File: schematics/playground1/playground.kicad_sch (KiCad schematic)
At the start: 98 parts, among them J1 Conn_01x05, J2 Conn_02x03_Odd_Even, J3 Conn_01x03, J4 Conn_02x04_Odd_Even, SW1 SW_SPST, SW2 SW_Push, SW3 SW_Push, U1 ADS1299, U2 MCP1700x-330xxTT, U3 PIC32MX250F128B_I_SS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

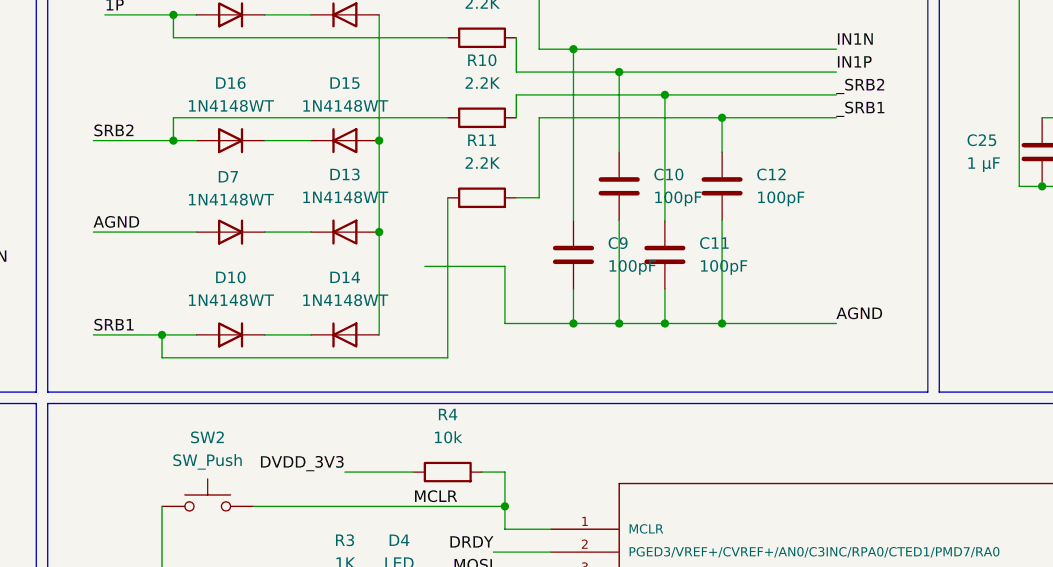
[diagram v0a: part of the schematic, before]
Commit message: add tracing for new resistor / diode arrays
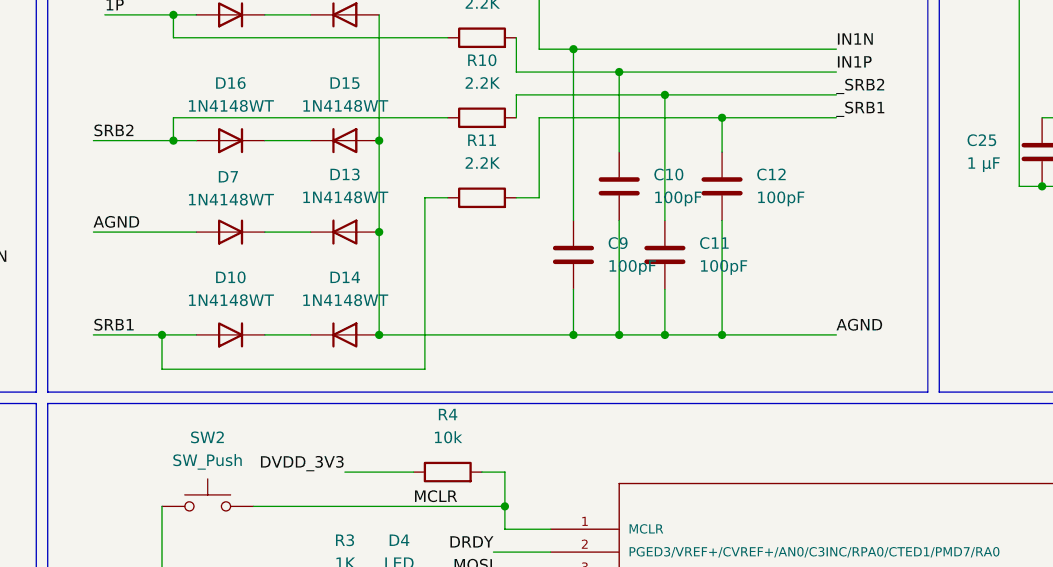
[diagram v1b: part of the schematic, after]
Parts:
- R10, R11, R8, R9: footprint (none) -> Resistor_SMD:R_0603_1608Metric
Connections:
- net AGND: now also D12.2 (A), D13.2 (A), D14.2 (A), D15.2 (A)
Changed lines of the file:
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@@
 	)
 	(junction
-		(at 153.67 162.56)
-		(diameter 0)
-		(color 0 0 0 0)
-	)
-	(junction
 		(at 251.46 45.72)
 		(diameter 0)
@@
 	)
 	(junction
-		(at 147.32 162.56)
-		(diameter 0)
-		(color 0 0 0 0)
-	)
-	(junction
 		(at 110.49 222.25)
 		(diameter 0)
@@
 	)
 	(junction
+		(at 137.16 163.83)
+		(diameter 0)
+		(color 0 0 0 0)
+	)
+	(junction
 		(at 91.44 86.36)
 		(diameter 0)
@@
 	)
 	(junction
-		(at 142.24 162.56)
-		(diameter 0)
-		(color 0 0 0 0)
-	)
-	(junction
 		(at 109.22 210.82)
 		(diameter 0)
@@
 	)
 	(junction
-		(at 137.16 162.56)
+		(at 281.94 115.57)
 		(diameter 0)
 		(color 0 0 0 0)
 	)
 	(junction
-		(at 281.94 115.57)
+		(at 91.44 163.83)
 		(diameter 0)
 		(color 0 0 0 0)
 	)
 	(junction
-		(at 91.44 163.83)
+		(at 142.24 163.83)
 		(diameter 0)
 		(color 0 0 0 0)
@@
 	)
 	(junction
+		(at 147.32 163.83)
+		(diameter 0)
+		(color 0 0 0 0)
+	)
+	(junction
 		(at 278.13 87.63)
 		(diameter 0)
@@
 	)
 	(junction
+		(at 115.57 163.83)
+		(diameter 0)
+		(color 0 0 0 0)
+	)
+	(junction
 		(at 91.44 43.18)
 		(diameter 0)
@@
 	)
 	(junction
+		(at 153.67 163.83)
+		(diameter 0)
+		(color 0 0 0 0)
+	)
+	(junction
 		(at 120.65 43.18)
 		(diameter 0)
@@
 	(wire
 		(pts
-			(xy 142.24 162.56) (xy 147.32 162.56)
+			(xy 142.24 163.83) (xy 147.32 163.83)
 		)
 		(stroke
@@
 	(wire
 		(pts
-			(xy 147.32 158.75) (xy 147.32 162.56)
-		)
-		(stroke
-			(width 0)
-			(type default)
-		)
-	)
-	(wire
-		(pts
 			(xy 208.28 147.32) (xy 219.71 147.32)
 		)
@@
 	(wire
 		(pts
-			(xy 120.65 156.21) (xy 129.54 156.21)
-		)
-		(stroke
-			(width 0)
-			(type default)
-		)
-	)
-	(wire
-		(pts
 			(xy 100.33 199.39) (xy 100.33 201.93)
 		)
@@
 	(wire
 		(pts
+			(xy 115.57 163.83) (xy 137.16 163.83)
+		)
+		(stroke
+			(width 0)
+			(type default)
+		)
+	)
+	(wire
+		(pts
 			(xy 116.84 43.18) (xy 120.65 43.18)
 		)
@@
 	(wire
 		(pts
-			(xy 91.44 163.83) (xy 91.44 166.37)
+			(xy 91.44 163.83) (xy 91.44 167.64)
 		)
 		(stroke
@@
 	(wire
 		(pts
-			(xy 129.54 162.56) (xy 137.16 162.56)
+			(xy 153.67 163.83) (xy 166.37 163.83)
 		)
 		(stroke
@@
 	(wire
 		(pts
-			(xy 153.67 162.56) (xy 166.37 162.56)
+			(xy 109.22 68.58) (xy 109.22 63.5)
 		)
 		(stroke
@@
 	(wire
 		(pts
-			(xy 109.22 68.58) (xy 109.22 63.5)
+			(xy 153.67 151.13) (xy 153.67 163.83)
 		)
 		(stroke
@@
 	(wire
 		(pts
-			(xy 153.67 162.56) (xy 153.67 151.13)
+			(xy 147.32 137.16) (xy 166.37 137.16)
 		)
 		(stroke
@@
 	(wire
 		(pts
-			(xy 147.32 137.16) (xy 166.37 137.16)
+			(xy 149.86 59.69) (xy 149.86 62.23)
 		)
 		(stroke
@@
 	(wire
 		(pts
-			(xy 149.86 59.69) (xy 149.86 62.23)
+			(xy 323.85 83.82) (xy 323.85 87.63)
 		)
 		(stroke
@@
 	(wire
 		(pts
-			(xy 323.85 83.82) (xy 323.85 87.63)
+			(xy 127 100.33) (xy 120.65 100.33)
 		)
 		(stroke
@@
 	(wire
 		(pts
-			(xy 127 100.33) (xy 120.65 100.33)
+			(xy 39.37 92.71) (xy 45.72 92.71)
 		)
 		(stroke
@@
 	(wire
 		(pts
-			(xy 39.37 92.71) (xy 45.72 92.71)
+			(xy 137.16 163.83) (xy 142.24 163.83)
 		)
 		(stroke
@@
 	(wire
 		(pts
-			(xy 137.16 162.56) (xy 142.24 162.56)
+			(xy 120.65 43.18) (xy 120.65 53.34)
 		)
 		(stroke
@@
 	(wire
 		(pts
-			(xy 120.65 43.18) (xy 120.65 53.34)
+			(xy 137.16 158.75) (xy 137.16 163.83)
 		)
 		(stroke
@@
 	(wire
 		(pts
-			(xy 147.32 162.56) (xy 153.67 162.56)
+			(xy 147.32 163.83) (xy 153.67 163.83)
 		)
 		(stroke
@@
 	(wire
 		(pts
-			(xy 142.24 151.13) (xy 142.24 162.56)
+			(xy 142.24 151.13) (xy 142.24 163.83)
 		)
 		(stroke
@@
 	(wire
 		(pts
+			(xy 147.32 158.75) (xy 147.32 163.83)
+		)
+		(stroke
+			(width 0)
+			(type default)
+		)
+	)
+	(wire
+		(pts
 			(xy 269.24 203.2) (xy 281.94 203.2)
 		)
@@
 	(wire
 		(pts
+			(xy 120.65 148.59) (xy 123.19 148.59)
+		)
+		(stroke
+			(width 0)
+			(type default)
+		)
+	)
+	(wire
+		(pts
 			(xy 91.44 80.01) (xy 101.6 80.01)
 		)
@@
 	(wire
 		(pts
-			(xy 123.19 166.37) (xy 91.44 166.37)
+			(xy 120.65 167.64) (xy 91.44 167.64)
 		)
 		(stroke
@@
 	(wire
 		(pts
-			(xy 137.16 158.75) (xy 137.16 162.56)
-		)
-		(stroke
-			(width 0)
-			(type default)
-		)
-	)
-	(wire
-		(pts
 			(xy 194.31 116.84) (xy 231.14 116.84)
 		)
@@
 	(wire
 		(pts
-			(xy 123.19 148.59) (xy 123.19 166.37)
+			(xy 120.65 148.59) (xy 120.65 167.64)
 		)
 		(stroke
@@
 	(wire
 		(pts
-			(xy 129.54 156.21) (xy 129.54 162.56)
-		)
-		(stroke
-			(width 0)
-			(type default)
-		)
-	)
-	(wire
-		(pts
 			(xy 248.92 144.78) (xy 246.38 144.78)
 		)
@@
 	)
 	(label "AGND"
-		(at 166.37 162.56 0)
+		(at 166.37 163.83 0)
 		(effects
 			(font
@@
 			)
 		)
-		(property "Footprint" ""
+		(property "Footprint" "Resistor_SMD:R_0603_1608Metric"
 			(at 127 150.368 90)
 			(effects
@@
 			)
 		)
-		(property "Footprint" ""
+		(property "Footprint" "Resistor_SMD:R_0603_1608Metric"
 			(at 127 123.698 90)
 			(effects
@@
 			)
 		)
-		(property "Footprint" ""
+		(property "Footprint" "Resistor_SMD:R_0603_1608Metric"
 			(at 127 141.478 90)
 			(effects
@@
 			)
 		)
-		(property "Footprint" ""
+		(property "Footprint" "Resistor_SMD:R_0603_1608Metric"
 			(at 127 132.588 90)
 			(effects

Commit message: traced pcb audio subsys edits
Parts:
- removed R6: 1k, Resistor_SMD:R_0603_1608Metric, symbol Device:R
- removed R7: 100k, Resistor_SMD:R_0603_1608Metric, symbol Device:R
- C40: value 1uF -> 0.1uF
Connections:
- net at U6.8 (VA): now also C40.1
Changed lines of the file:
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@@
 	)
 	(junction
-		(at 368.3 189.23)
-		(diameter 0)
-		(color 0 0 0 0)
-	)
-	(junction
 		(at 189.23 107.95)
 		(diameter 0)
@@
 	(wire
 		(pts
-			(xy 368.3 168.91) (xy 368.3 167.64)
-		)
-		(stroke
-			(width 0)
-			(type default)
-		)
-	)
-	(wire
-		(pts
 			(xy 100.33 199.39) (xy 100.33 201.93)
 		)
@@
 	(wire
 		(pts
-			(xy 347.98 189.23) (xy 356.87 189.23)
-		)
-		(stroke
-			(width 0)
-			(type default)
-		)
-	)
-	(wire
-		(pts
 			(xy 45.72 90.17) (xy 39.37 90.17)
 		)
@@
 	(wire
 		(pts
+			(xy 368.3 167.64) (xy 368.3 177.8)
+		)
+		(stroke
+			(width 0)
+			(type default)
+		)
+	)
+	(wire
+		(pts
 			(xy 130.81 130.81) (xy 130.81 134.62)
 		)
@@
 	(wire
 		(pts
-			(xy 368.3 176.53) (xy 368.3 177.8)
-		)
-		(stroke
-			(width 0)
-			(type default)
-		)
-	)
-	(wire
-		(pts
 			(xy 120.65 208.28) (xy 134.62 208.28)
 		)
@@
 	(wire
 		(pts
-			(xy 364.49 189.23) (xy 368.3 189.23)
-		)
-		(stroke
-			(width 0)
-			(type default)
-		)
-	)
-	(wire
-		(pts
 			(xy 100.33 210.82) (xy 109.22 210.82)
 		)
@@
 	)
 	(symbol
-		(lib_id "Device:R")
-		(at 368.3 172.72 0)
-		(unit 1)
-		(exclude_from_sim no)
-		(in_bom yes)
-		(on_board yes)
-		(dnp no)
-		(fields_autoplaced yes)
-		(property "Reference" "R6"
-			(at 370.84 171.4499 0)
-			(effects
-				(font
-					(size 1.27 1.27)
-				)
-				(justify left)
-			)
-		)
-		(property "Value" "1k"
-			(at 370.84 173.9899 0)
-			(effects
-				(font
-					(size 1.27 1.27)
-				)
-				(justify left)
-			)
-		)
-		(property "Footprint" "Resistor_SMD:R_0603_1608Metric"
-			(at 366.522 172.72 90)
-			(effects
-				(font
-					(size 1.27 1.27)
-				)
-				(hide yes)
-			)
-		)
-		(property "Datasheet" "~"
-			(at 368.3 172.72 0)
-			(effects
-				(font
-					(size 1.27 1.27)
-				)
-				(hide yes)
-			)
-		)
-		(property "Description" "Resistor"
-			(at 368.3 172.72 0)
-			(effects
-				(font
-					(size 1.27 1.27)
-				)
-				(hide yes)
-			)
-		)
-		(pin "2"
-		)
-		(pin "1"
-		)
-		(instances
-			(project "playground"
-				(path "/238de170-6a90-40ad-afaf-ab931b754487"
-					(reference "R6")
-					(unit 1)
-				)
-			)
-		)
-	)
-	(symbol
 		(lib_id "ble_symbols:C")
 		(at 200.66 135.89 0)
@@
 	)
 	(symbol
-		(lib_id "Device:R")
-		(at 360.68 189.23 270)
-		(mirror x)
-		(unit 1)
-		(exclude_from_sim no)
-		(in_bom yes)
-		(on_board yes)
-		(dnp no)
-		(property "Reference" "R7"
-			(at 360.68 182.88 90)
-			(effects
-				(font
-					(size 1.27 1.27)
-				)
-			)
-		)
-		(property "Value" "100k"
-			(at 360.68 185.42 90)
-			(effects
-				(font
-					(size 1.27 1.27)
-				)
-			)
-		)
-		(property "Footprint" "Resistor_SMD:R_0603_1608Metric"
-			(at 360.68 191.008 90)
-			(effects
-				(font
-					(size 1.27 1.27)
-				)
-				(hide yes)
-			)
-		)
-		(property "Datasheet" "~"
-			(at 360.68 189.23 0)
-			(effects
-				(font
-					(size 1.27 1.27)
-				)
-				(hide yes)
-			)
-		)
-		(property "Description" "Resistor"
-			(at 360.68 189.23 0)
-			(effects
-				(font
-					(size 1.27 1.27)
-				)
-				(hide yes)
-			)
-		)
-		(pin "2"
-		)
-		(pin "1"
-		)
-		(instances
-			(project "playground"
-				(path "/238de170-6a90-40ad-afaf-ab931b754487"
-					(reference "R7")
-					(unit 1)
-				)
-			)
-		)
-	)
-	(symbol
 		(lib_id "ble_symbols:C")
 		(at 189.23 143.51 0)
@@
 			)
 		)
-		(property "Value" "1uF"
+		(property "Value" "0.1uF"
 			(at 372.11 182.8799 0)
 			(effects
